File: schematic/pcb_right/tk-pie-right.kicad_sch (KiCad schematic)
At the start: 35 parts, among them IC1 PCA9539PW,118, J1 NiceView, J2 Battery Connector, U3 SN74LVC1T45DCK

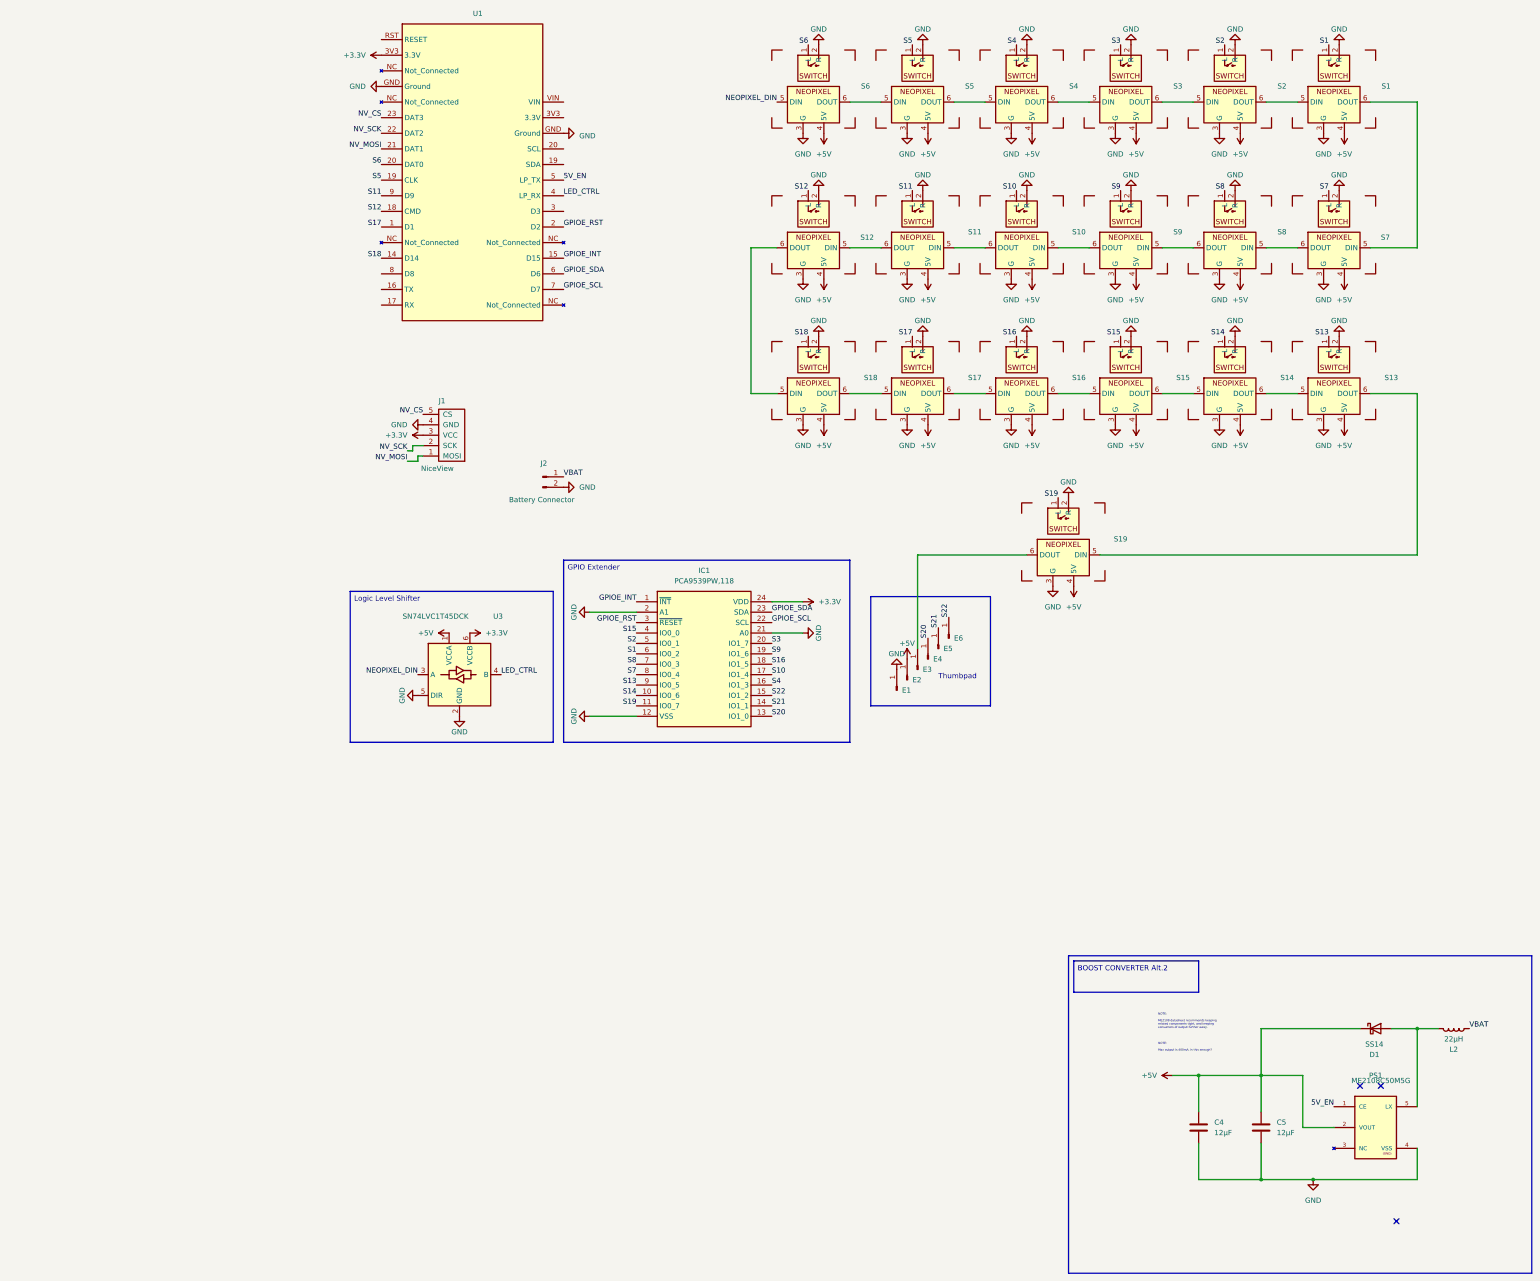
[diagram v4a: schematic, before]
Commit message: pcb-right: Add through-holes to vbat pads
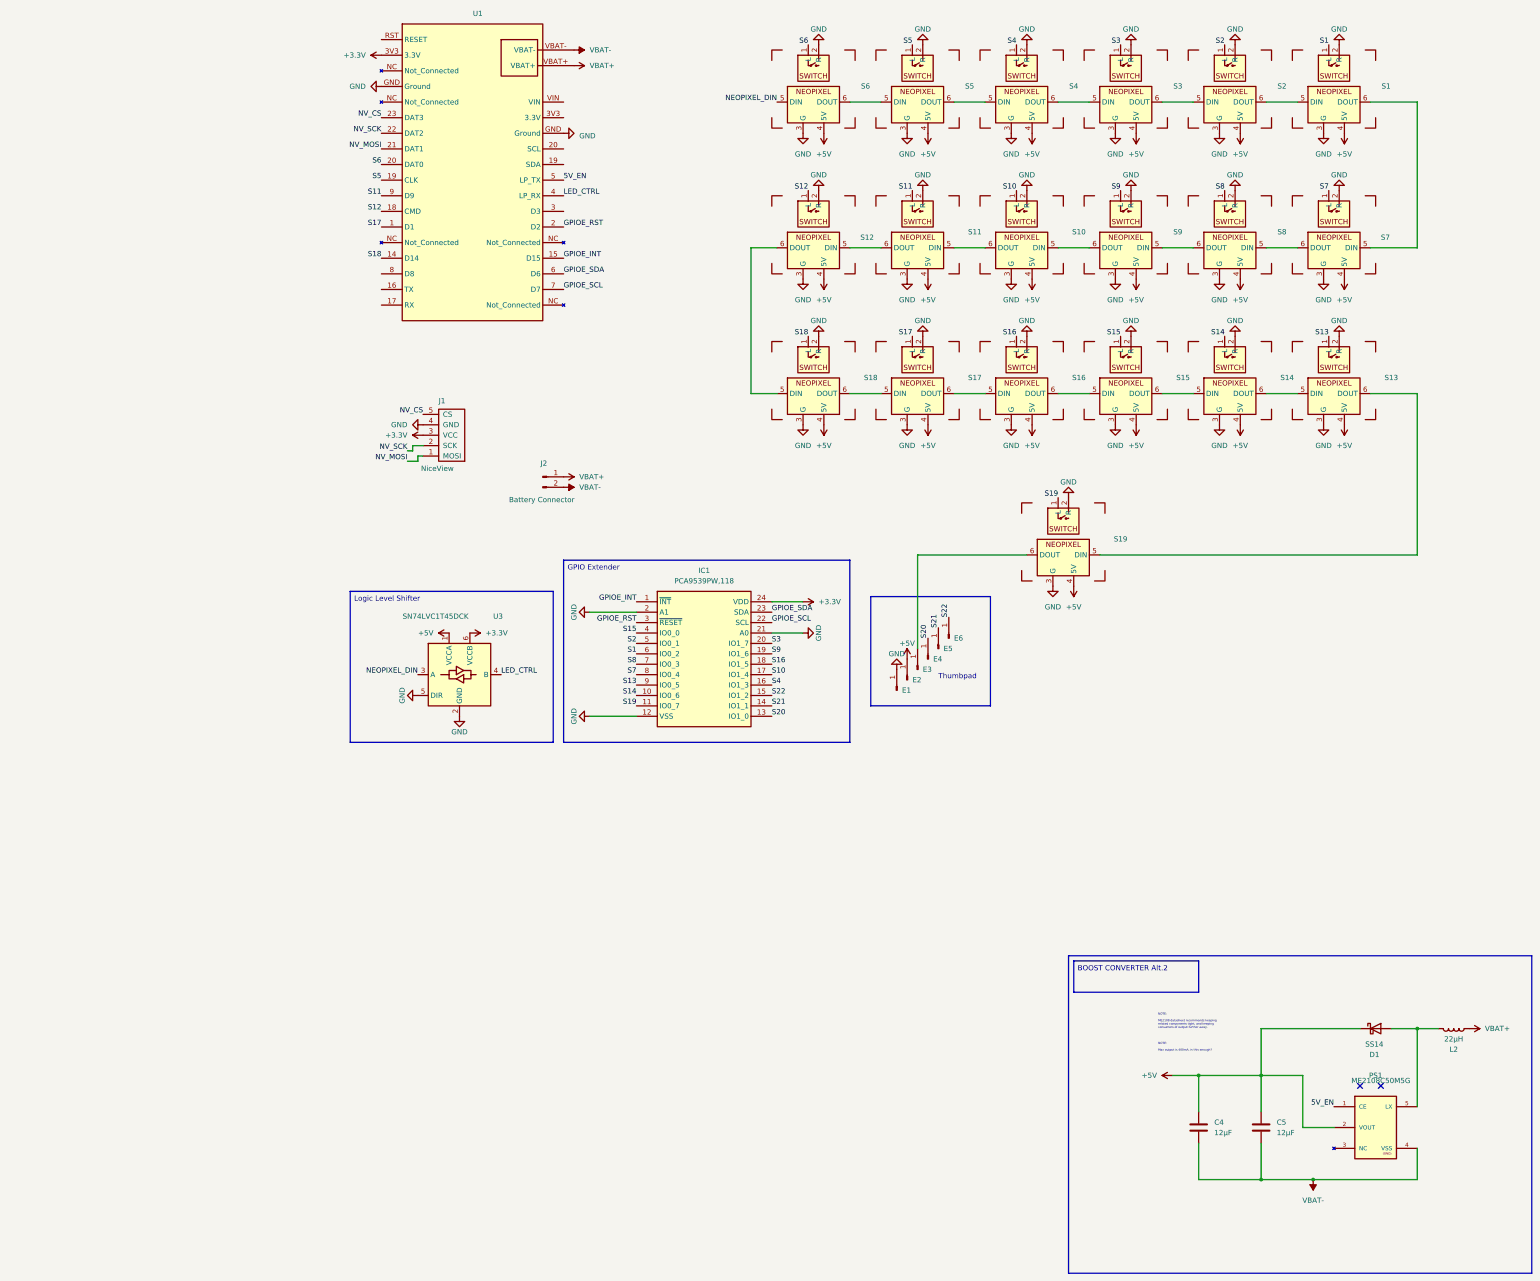
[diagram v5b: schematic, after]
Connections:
- net GND: no longer C4.2, C5.1, J2.2 (Pin_2), PS1.4 (VSS)
- net VBAT renamed VBAT+
- net VBAT+: now also U1.VBAT+
- new net VBAT-: C4.2, C5.1, J2.2 (Pin_2), PS1.4 (VSS), U1.VBAT-
- no-connect marks 3 -> 2
